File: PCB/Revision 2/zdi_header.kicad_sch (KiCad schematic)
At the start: 4 parts, among them J5 Conn_02x03_Odd_Even

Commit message: Work on the schematic continutes
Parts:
- removed R34, R35: 10KΩ, symbol Turaco:R
- added RN2: 10KΩ, symbol Device:R_Pack04_Split
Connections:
- net TCK: now also RN2.6 (R3.2)
- net VCC: now also RN2.3 (R3.1), RN2.4 (R4.1)
- net ~{RESET}: now also RN2.5 (R4.2)
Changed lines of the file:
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@@
     (effects (font (size 1.27 1.27)) (justify left))
-  )
-  (symbol (lib_id "Turaco:R") (at 130.81 85.09 0) (unit 1)
-    (in_bom yes) (on_board yes) (dnp no) (fields_autoplaced)
-    (property "Reference" "R34" (at 133.35 83.8199 0)
-      (effects (font (size 1.27 1.27)) (justify left))
-    )
-    (property "Value" "10KΩ" (at 133.35 86.3599 0)
-      (effects (font (size 1.27 1.27)) (justify left))
-    )
-    (property "Footprint" "" (at 129.032 85.09 90)
-      (effects (font (size 1.27 1.27)) hide)
-    )
-    (property "Datasheet" "~" (at 130.81 85.09 0)
-      (effects (font (size 1.27 1.27)) hide)
-    )
-    (pin "1")
-    (pin "2")
-    (instances
-      (project "Revision 2"
-        (path "/3ba39048-ccb5-49b6-bc29-f9a8dd2e53b6/c07b2ed0-3ddf-4a7b-83a6-b9bc424f9605"
-          (reference "R34") (unit 1)
-        )
-      )
-    )
   )
   (symbol (lib_id "power:VCC") (at 148.59 78.74 0) (unit 1)
@@
         (path "/3ba39048-ccb5-49b6-bc29-f9a8dd2e53b6/c07b2ed0-3ddf-4a7b-83a6-b9bc424f9605"
           (reference "#PWR0122") (unit 1)
+        )
+      )
+    )
+  )
+  (symbol (lib_id "Device:R_Pack04_Split") (at 139.7 85.09 180) (unit 3)
+    (in_bom yes) (on_board yes) (dnp no)
+    (property "Reference" "RN2" (at 141.5821 85.0457 90)
+      (effects (font (size 1.27 1.27)))
+    )
+    (property "Value" "10KΩ" (at 139.7 85.09 90)
+      (effects (font (size 1.27 1.27)))
+    )
+    (property "Footprint" "" (at 141.732 85.09 90)
+      (effects (font (size 1.27 1.27)) hide)
+    )
+    (property "Datasheet" "~" (at 139.7 85.09 0)
+      (effects (font (size 1.27 1.27)) hide)
+    )
+    (pin "1")
+    (pin "8")
+    (pin "2")
+    (pin "7")
+    (pin "3")
+    (pin "6")
+    (pin "4")
+    (pin "5")
+    (instances
+      (project "Revision 2"
+        (path "/3ba39048-ccb5-49b6-bc29-f9a8dd2e53b6/e0049583-c97a-4b82-a4d7-59c894eac2f8"
+          (reference "RN2") (unit 3)
+        )
+        (path "/3ba39048-ccb5-49b6-bc29-f9a8dd2e53b6/8eb73f8e-3afe-409d-b449-f86a2b765fba"
+          (reference "RN7") (unit 3)
+        )
+        (path "/3ba39048-ccb5-49b6-bc29-f9a8dd2e53b6/c07b2ed0-3ddf-4a7b-83a6-b9bc424f9605"
+          (reference "RN7") (unit 3)
         )
       )
@@
     )
   )
-  (symbol (lib_id "Turaco:R") (at 139.7 85.09 0) (unit 1)
-    (in_bom yes) (on_board yes) (dnp no) (fields_autoplaced)
-    (property "Reference" "R35" (at 142.24 83.8199 0)
-      (effects (font (size 1.27 1.27)) (justify left))
+  (symbol (lib_id "Device:R_Pack04_Split") (at 130.81 85.09 180) (unit 4)
+    (in_bom yes) (on_board yes) (dnp no)
+    (property "Reference" "RN2" (at 132.6586 85.0084 90)
+      (effects (font (size 1.27 1.27)))
     )
-    (property "Value" "10KΩ" (at 142.24 86.3599 0)
-      (effects (font (size 1.27 1.27)) (justify left))
+    (property "Value" "10KΩ" (at 130.81 85.09 90)
+      (effects (font (size 1.27 1.27)))
     )
-    (property "Footprint" "" (at 137.922 85.09 90)
+    (property "Footprint" "" (at 132.842 85.09 90)
       (effects (font (size 1.27 1.27)) hide)
     )
-    (property "Datasheet" "~" (at 139.7 85.09 0)
+    (property "Datasheet" "~" (at 130.81 85.09 0)
       (effects (font (size 1.27 1.27)) hide)
     )
     (pin "1")
+    (pin "8")
     (pin "2")
+    (pin "7")
+    (pin "3")
+    (pin "6")
+    (pin "4")
+    (pin "5")
     (instances
       (project "Revision 2"
+        (path "/3ba39048-ccb5-49b6-bc29-f9a8dd2e53b6/e0049583-c97a-4b82-a4d7-59c894eac2f8"
+          (reference "RN2") (unit 4)
+        )
+        (path "/3ba39048-ccb5-49b6-bc29-f9a8dd2e53b6/8eb73f8e-3afe-409d-b449-f86a2b765fba"
+          (reference "RN7") (unit 4)
+        )
         (path "/3ba39048-ccb5-49b6-bc29-f9a8dd2e53b6/c07b2ed0-3ddf-4a7b-83a6-b9bc424f9605"
-          (reference "R35") (unit 1)
+          (reference "RN7") (unit 4)
         )
       )

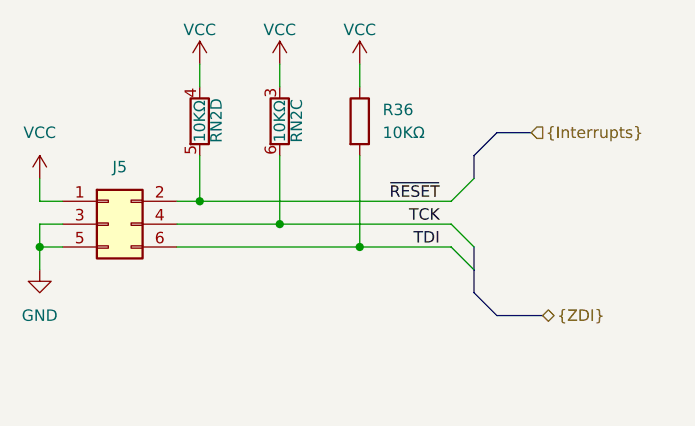
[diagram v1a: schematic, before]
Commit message: ESD protection diodes go BRRRRRRR
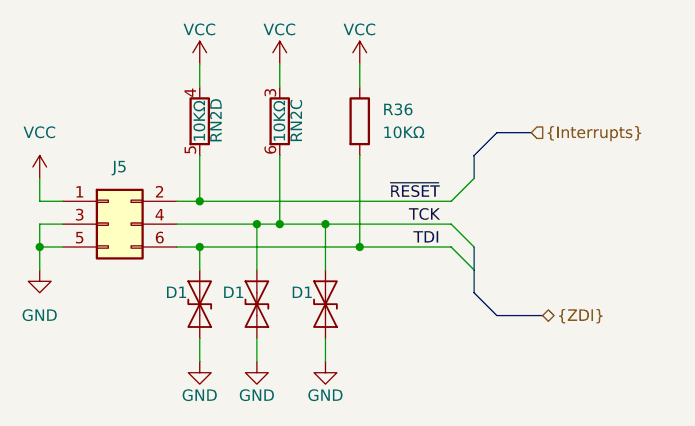
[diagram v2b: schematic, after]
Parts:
- added D1 (x3): ESD9B3.3ST5G, Diode_SMD:D_SOD-923, symbol Diode:ESD9B3.3ST5G
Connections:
- net GND: now also D1.2 (A2), D1.2 (A2), D1.2 (A2)
- net TCK: now also D1.1 (A1), D1.1 (A1)
- net TDI: now also D1.1 (A1)

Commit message: Updated re: issue #2
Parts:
- RN2: footprint (none) -> Resistor_SMD:R_Array_Concave_4x0402
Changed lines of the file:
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@@
       (effects (font (size 1.27 1.27)))
     )
-    (property "Footprint" "" (at 141.732 85.09 90)
+    (property "Footprint" "Resistor_SMD:R_Array_Concave_4x0402" (at 141.732 85.09 90)
       (effects (font (size 1.27 1.27)) hide)
     )
@@
       (effects (font (size 1.27 1.27)))
     )
-    (property "Footprint" "" (at 132.842 85.09 90)
-      (effects (font (size 1.27 1.27)) hide)
-    )
+    (property "Footprint" "Resistor_SMD:R_Array_Concave_4x0402" (at 132.842 85.09 90)
+      (effects (font (size 1.27 1.27)) hide)
+    )
